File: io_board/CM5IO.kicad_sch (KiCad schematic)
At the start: 4 parts, among them J11 USB_C_Receptacle_USB2.0

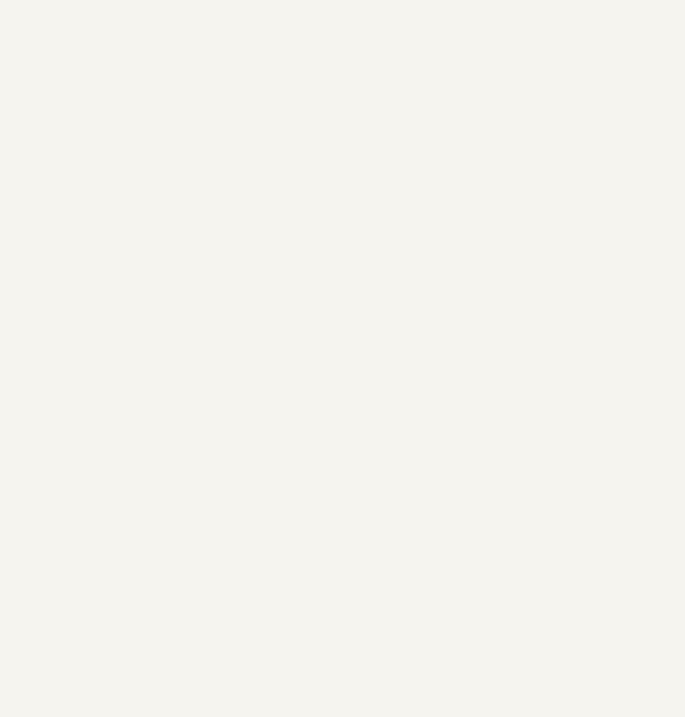
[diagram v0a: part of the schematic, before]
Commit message: Added all necessary IO connectors.
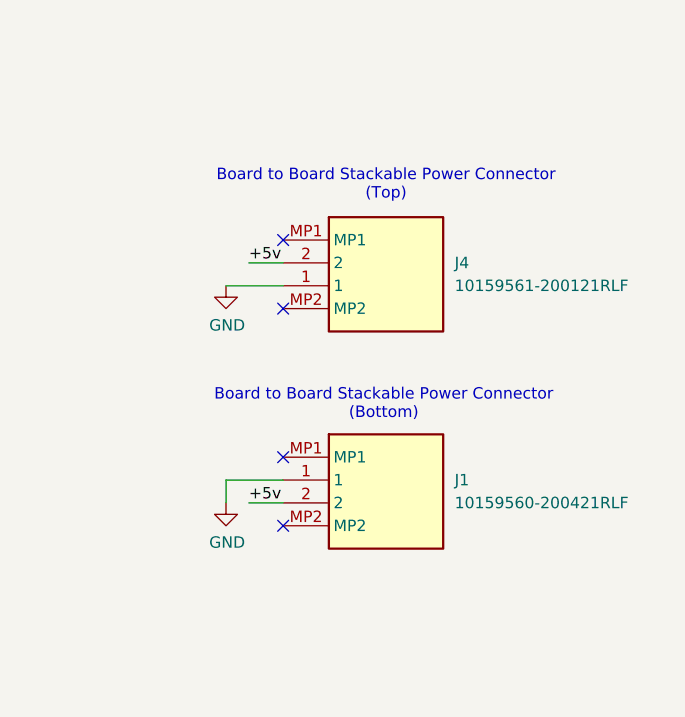
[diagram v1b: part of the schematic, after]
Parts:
- added J1: 10159560-200421RLF, 10159560-200421RLF:10159560200421RLF, symbol 10159560-200421RLF:10159560-200421RLF
- added J4: 10159561-200121RLF, 10159561-200121RLF:10159561200121RLF, symbol 10159561-200121RLF:10159561-200121RLF
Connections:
- net +5v: now also J1.2, J4.2
- net GND: now also J1.1, J4.1
- no-connect marks 12 -> 16
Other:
- note added: "Board to Board Stackable Power Connector (Bottom)"
- note added: "Board to Board Stackable Power Connector (Top)"

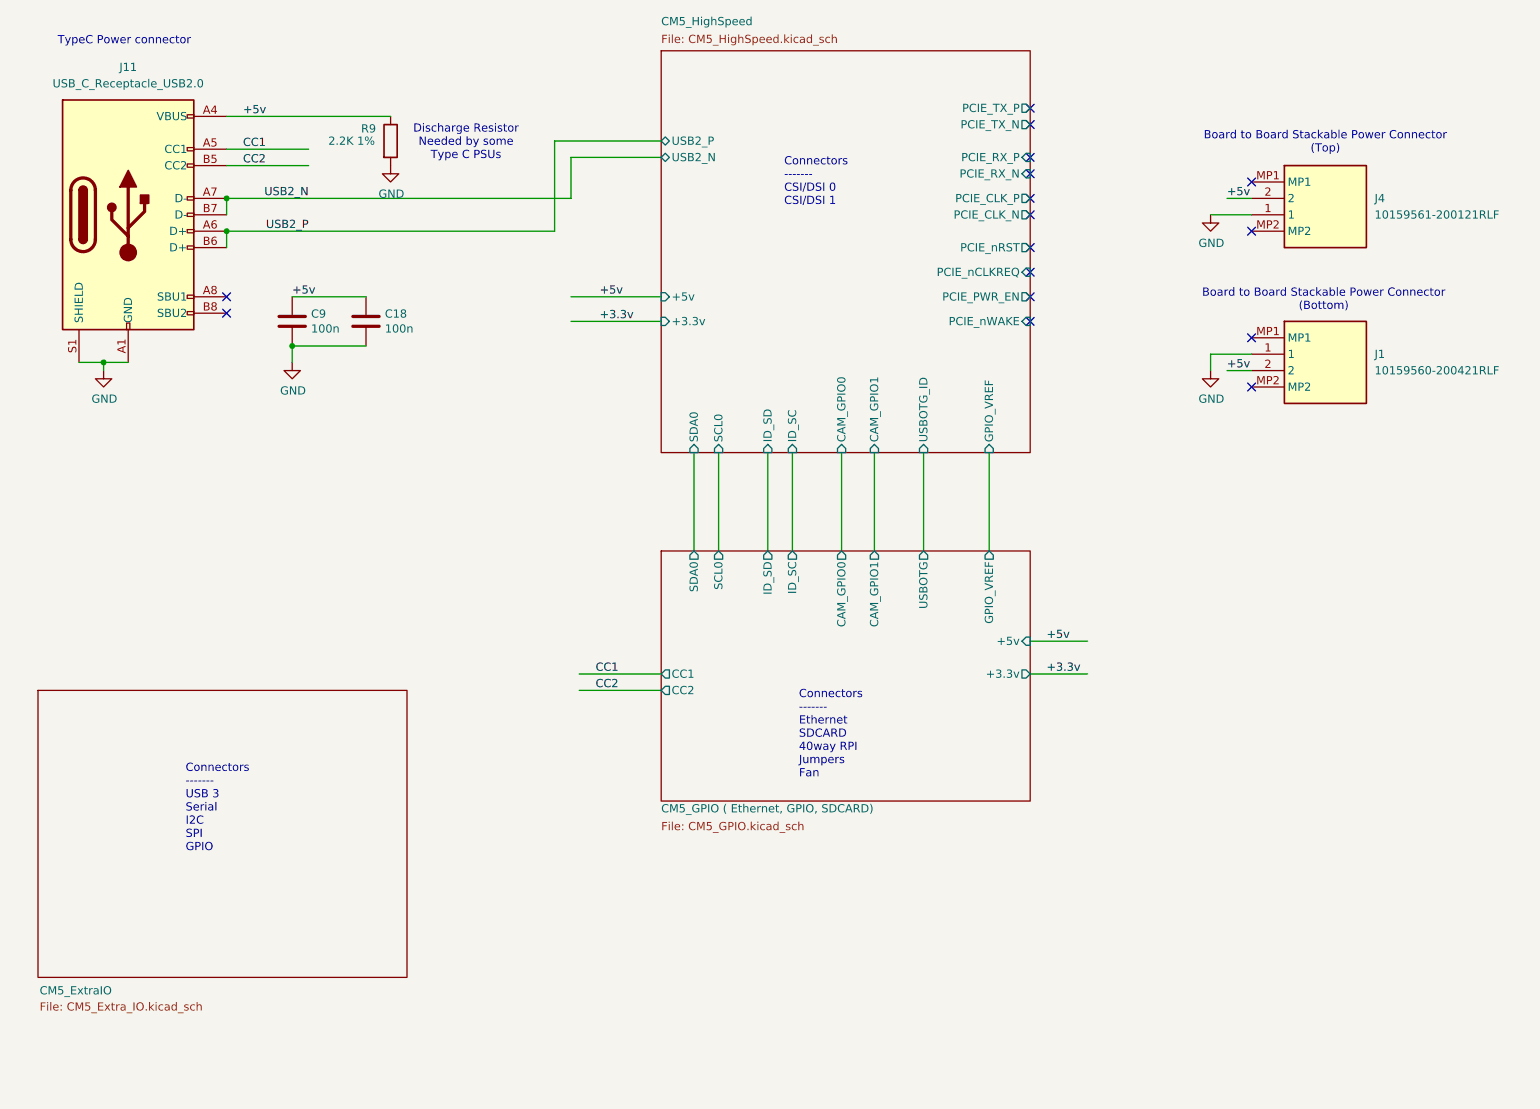
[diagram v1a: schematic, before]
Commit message: Assigned pins to I2C, UART, PWM, SPI ports.
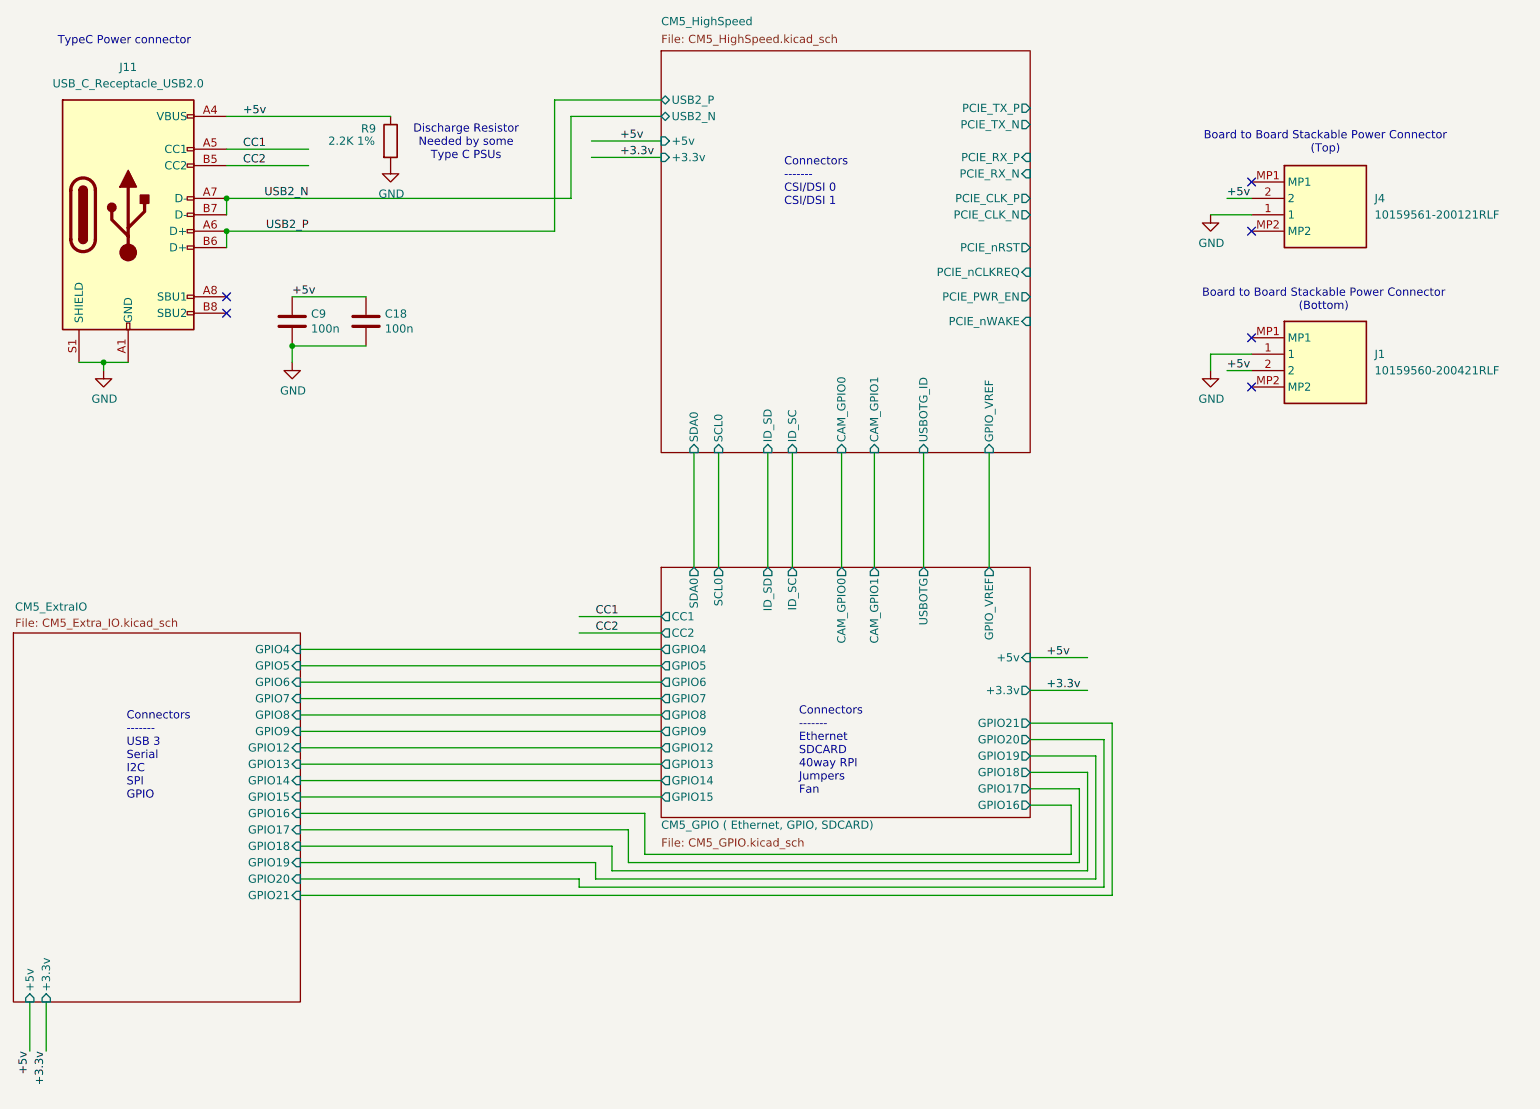
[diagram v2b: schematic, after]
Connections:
- no-connect marks 16 -> 6
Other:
- sheet CM5_ExtraIO ports: added +3.3v, +5v, GPIO12, GPIO13, GPIO14, GPIO15, GPIO16, GPIO17, GPIO18, GPIO19, GPIO20, GPIO21, GPIO4, GPIO5, GPIO6, GPIO7, GPIO8, GPIO9; removed none
- sheet CM5_GPIO ( Ethernet, GPIO, SDCARD) ports: added GPIO12, GPIO13, GPIO14, GPIO15, GPIO16, GPIO17, GPIO18, GPIO19, GPIO20, GPIO21, GPIO4, GPIO5, GPIO6, GPIO7, GPIO8, GPIO9; removed none

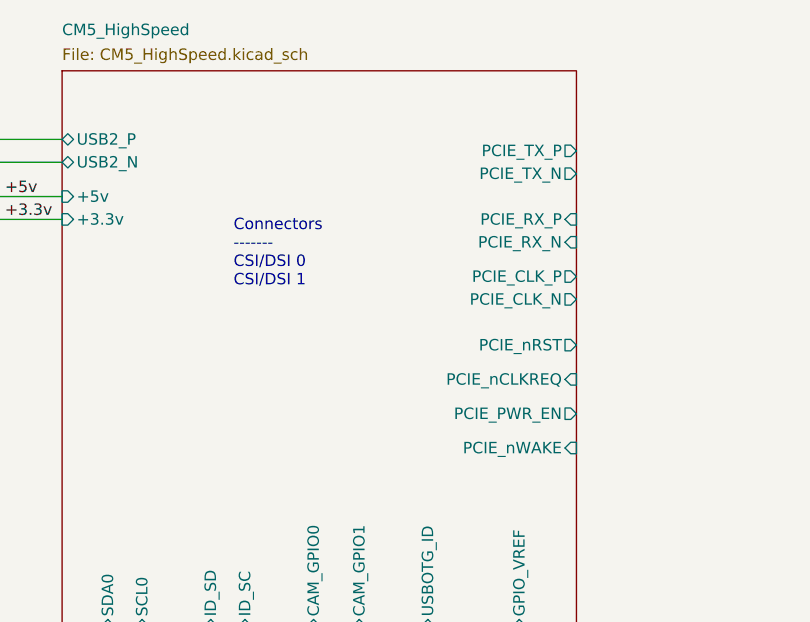
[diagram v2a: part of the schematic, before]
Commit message: Connected USB 3.0 and added part number for PCIe.
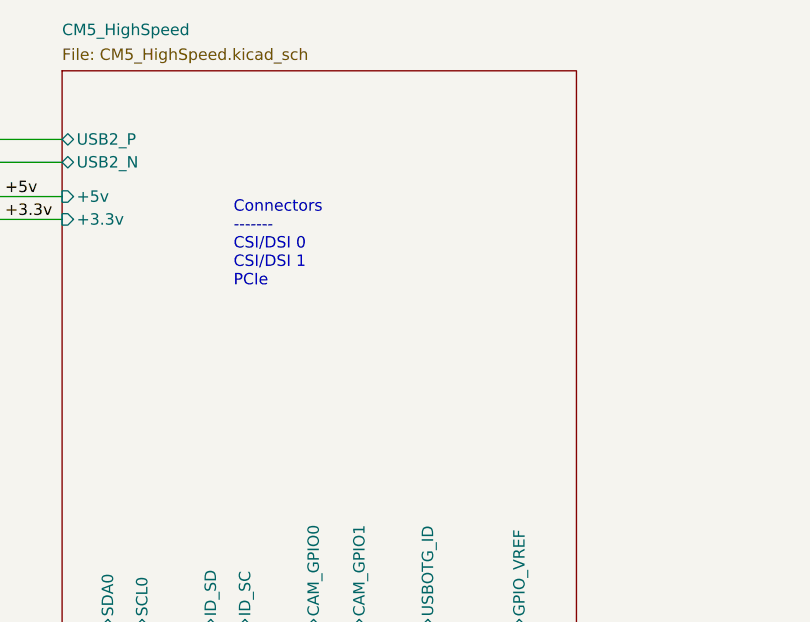
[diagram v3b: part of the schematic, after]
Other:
- sheet CM5_HighSpeed ports: added none; removed PCIE_CLK_N, PCIE_CLK_P, PCIE_PWR_EN, PCIE_RX_N, PCIE_RX_P, PCIE_TX_N, PCIE_TX_P, PCIE_nCLKREQ, PCIE_nRST, PCIE_nWAKE
- note added: "Connectors ------- CSI/DSI 0 CSI/DSI 1 PCIe"
- note removed: "Connectors ------- CSI/DSI 0 CSI/DSI 1"
- company: Copyright © 2024 Raspberry Pi Ltd. -> Copyright © 2024 Raspberry Pi Ltd. & Ilias Kringos
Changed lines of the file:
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@@
 		(title "Compute Module 5 IO Board - Top Level")
 		(rev "1")
-		(company "Copyright © 2024 Raspberry Pi Ltd.")
+		(company "Copyright © 2024 Raspberry Pi Ltd. & Ilias Kringos")
 		(comment 1 "www.raspberrypi.com")
 	)
@@
 		)
 	)
-	(text "Connectors\n-------\nCSI/DSI 0\nCSI/DSI 1"
+	(text "Connectors\n-------\nCSI/DSI 0\nCSI/DSI 1\nPCIe"
 		(exclude_from_sim no)
 		(at 148.59 58.42 0)
@@
 			)
 		)
-		(pin "PCIE_CLK_P" output
-			(at 186.69 57.15 0)
-			(effects
-				(font
-					(size 1.27 1.27)
-				)
-				(justify right)
-			)
-		)
-		(pin "PCIE_CLK_N" output
-			(at 186.69 59.69 0)
-			(effects
-				(font
-					(size 1.27 1.27)
-				)
-				(justify right)
-			)
-		)
-		(pin "PCIE_TX_P" output
-			(at 186.69 43.18 0)
-			(effects
-				(font
-					(size 1.27 1.27)
-				)
-				(justify right)
-			)
-		)
-		(pin "PCIE_TX_N" output
-			(at 186.69 45.72 0)
-			(effects
-				(font
-					(size 1.27 1.27)
-				)
-				(justify right)
-			)
-		)
-		(pin "PCIE_nRST" output
-			(at 186.69 64.77 0)
-			(effects
-				(font
-					(size 1.27 1.27)
-				)
-				(justify right)
-			)
-		)
-		(pin "PCIE_RX_P" input
-			(at 186.69 50.8 0)
-			(effects
-				(font
-					(size 1.27 1.27)
-				)
-				(justify right)
-			)
-		)
-		(pin "PCIE_RX_N" input
-			(at 186.69 53.34 0)
-			(effects
-				(font
-					(size 1.27 1.27)
-				)
-				(justify right)
-			)
-		)
-		(pin "PCIE_nCLKREQ" input
-			(at 186.69 68.58 0)
-			(effects
-				(font
-					(size 1.27 1.27)
-				)
-				(justify right)
-			)
-		)
 		(pin "+3.3v" input
 			(at 129.54 50.8 180)
@@
 			)
 		)
-		(pin "PCIE_PWR_EN" output
-			(at 186.69 72.39 0)
-			(effects
-				(font
-					(size 1.27 1.27)
-				)
-				(justify right)
-			)
-		)
-		(pin "PCIE_nWAKE" input
-			(at 186.69 76.2 0)
-			(effects
-				(font
-					(size 1.27 1.27)
-				)
-				(justify right)
-			)
-		)
